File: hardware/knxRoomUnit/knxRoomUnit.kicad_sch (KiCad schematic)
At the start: 0 parts

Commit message: Initial hardware commit
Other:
- removed sheet KNX

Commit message: Hardware Update
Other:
- sheet MCU renamed MCU-KNX
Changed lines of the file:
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@@
     (stroke (width 0) (type solid))
     (fill (color 0 0 0 0.0000))
-    (property "Sheetname" "MCU" (at 21.59 20.8784 0)
+    (property "Sheetname" "MCU-KNX" (at 21.59 20.8784 0)
       (effects (font (size 1.27 1.27)) (justify left bottom))
     )

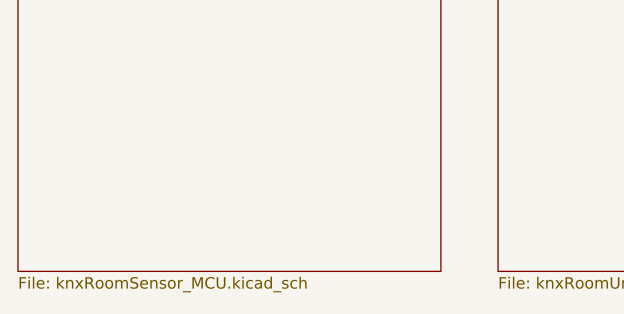
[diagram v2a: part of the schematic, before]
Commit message: Updated sensors
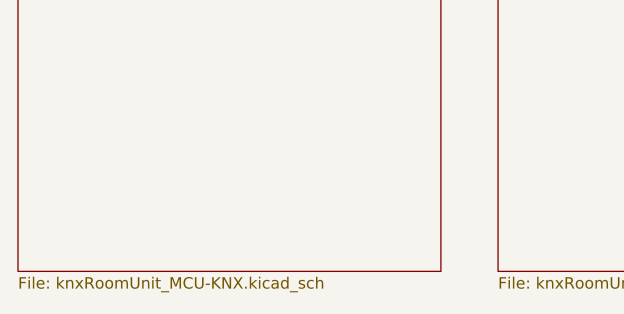
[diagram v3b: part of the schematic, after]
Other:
- sheet MCU-KNX: file knxRoomSensor_MCU.kicad_sch -> knxRoomUnit_MCU-KNX.kicad_sch
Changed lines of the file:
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@@
       (effects (font (size 1.27 1.27)) (justify left bottom))
     )
-    (property "Sheetfile" "knxRoomSensor_MCU.kicad_sch" (at 21.59 69.1646 0)
+    (property "Sheetfile" "knxRoomUnit_MCU-KNX.kicad_sch" (at 21.59 69.1646 0)
       (effects (font (size 1.27 1.27)) (justify left top))
     )
